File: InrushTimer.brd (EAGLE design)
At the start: 62.2 x 36 mm, 72 parts, among them IC1 TLC272D, IC2 555, IC3 4076N, Q2 TRANSISTOR-FET_2N7002, Q3 TRANSISTOR-FET_2N7002, Q4 TRANSISTOR-FET_2N7002, Q5 TRANSISTOR-FET_2N7002, Q6 DIODES_ZTX451DIODES_ZTX451_0_0, T1 MMBTA05, U1 ROHM_BY_ELEMENT14_BATCH_1_BU4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

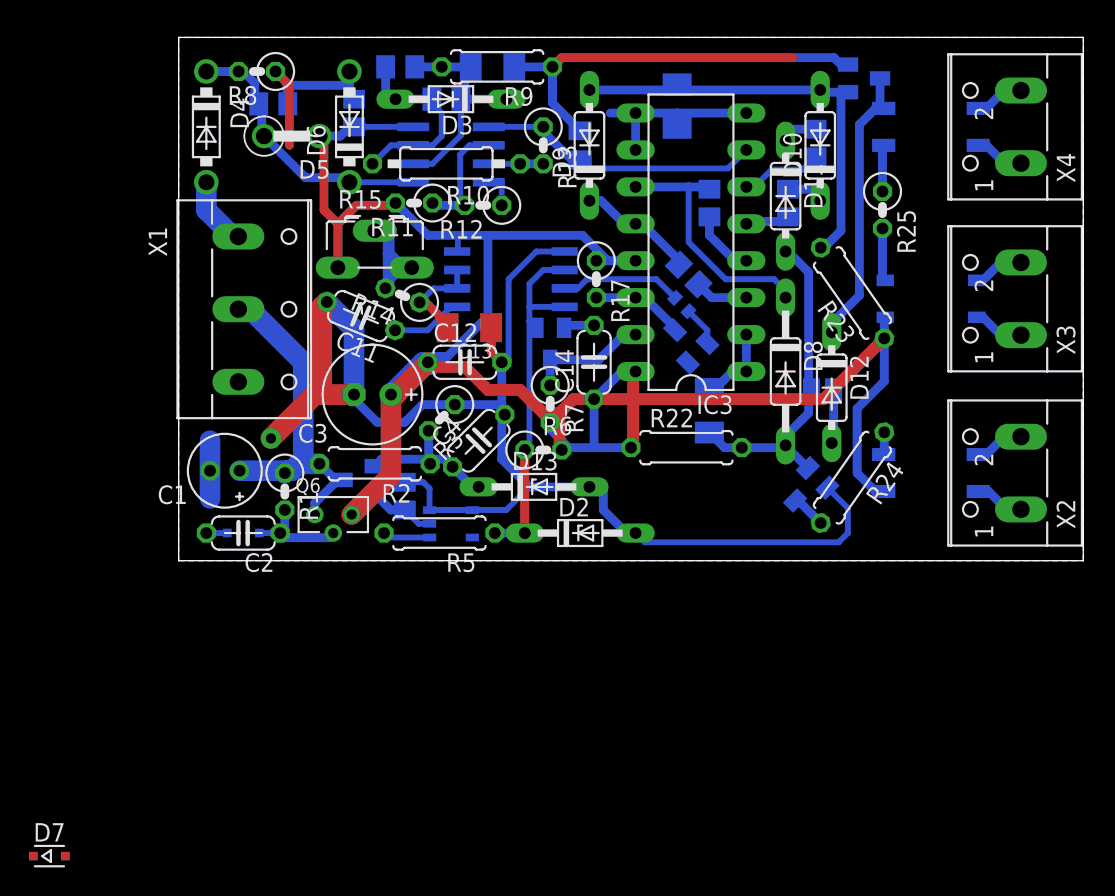
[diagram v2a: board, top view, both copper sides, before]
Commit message: Tidied up component and track placement.
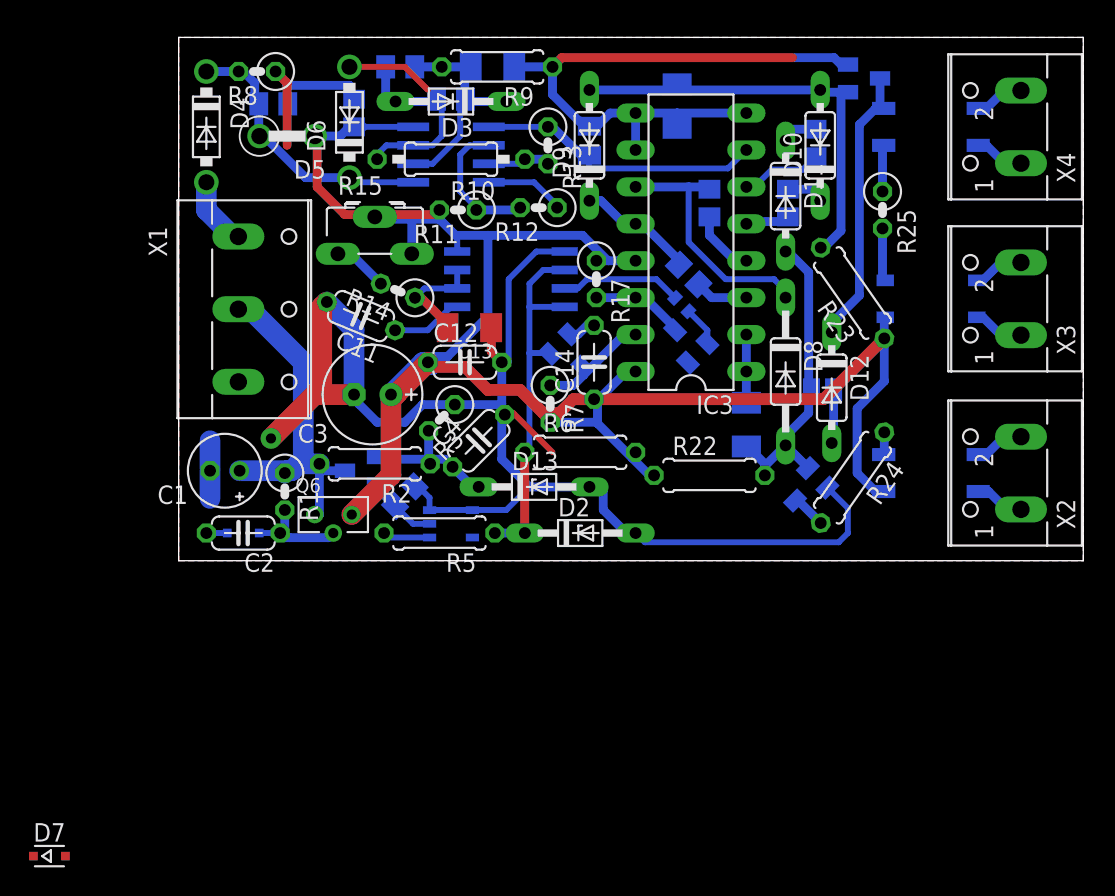
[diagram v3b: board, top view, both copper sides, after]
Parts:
- R6: device rcl:0207/2V -> rcl:0207/7
- moved R12 3.81 mm to (24.8, 24.3)
- moved R11 3.05 mm to (19.2, 24.1)
- moved C15 2.71 mm to (39.1, 9.37)
- moved R6 2.54 mm to (27.6, 7.46)
- moved R22 2.48 mm to (36.5, 5.87)
- moved Q2 1.63 mm to (27.0, 14.1), turned to 135 degrees
- moved R15 0.95 mm to (13.5, 21.1)
- moved C10 0.71 mm to (28.3, 28.9)
- moved T1 0.65 mm to (12.5, 6.19)
- moved R10 0.45 mm to (18.7, 27.6)
- moved R14 0.45 mm to (15.1, 18.6)
- moved C7 0.32 mm to (18.7, 31.8)
- moved D6 0.32 mm to (11.7, 30.2)
- moved D5 0.32 mm to (7.46, 29.2)
- moved R13 0.32 mm to (25.4, 28.6)
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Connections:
- removed net N$2: R14.2, R15.E, R15.S
- new net N$34: R14.2, R15.A
- net V12: now also R15.E, R15.S; no longer R15.A
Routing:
- net V12: track 153.5 -> 140.6 mm
- net ZERO: track 185.4 -> 195.3 mm
- net N$2: track 8.40 -> 0.00 mm
- net N$34: track 0.00 -> 3.80 mm
- net THRESH: track 8.14 -> 9.67 mm
- net ON_A_SYNC: track 22.9 -> 21.8 mm
- net RECT: track 24.0 -> 24.9 mm
- net RESET_N: track 25.3 -> 26.0 mm
- net N$28: track 7.04 -> 7.68 mm
- net N$26: track 3.75 -> 4.33 mm

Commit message: Rev two layout - minor change to track angle
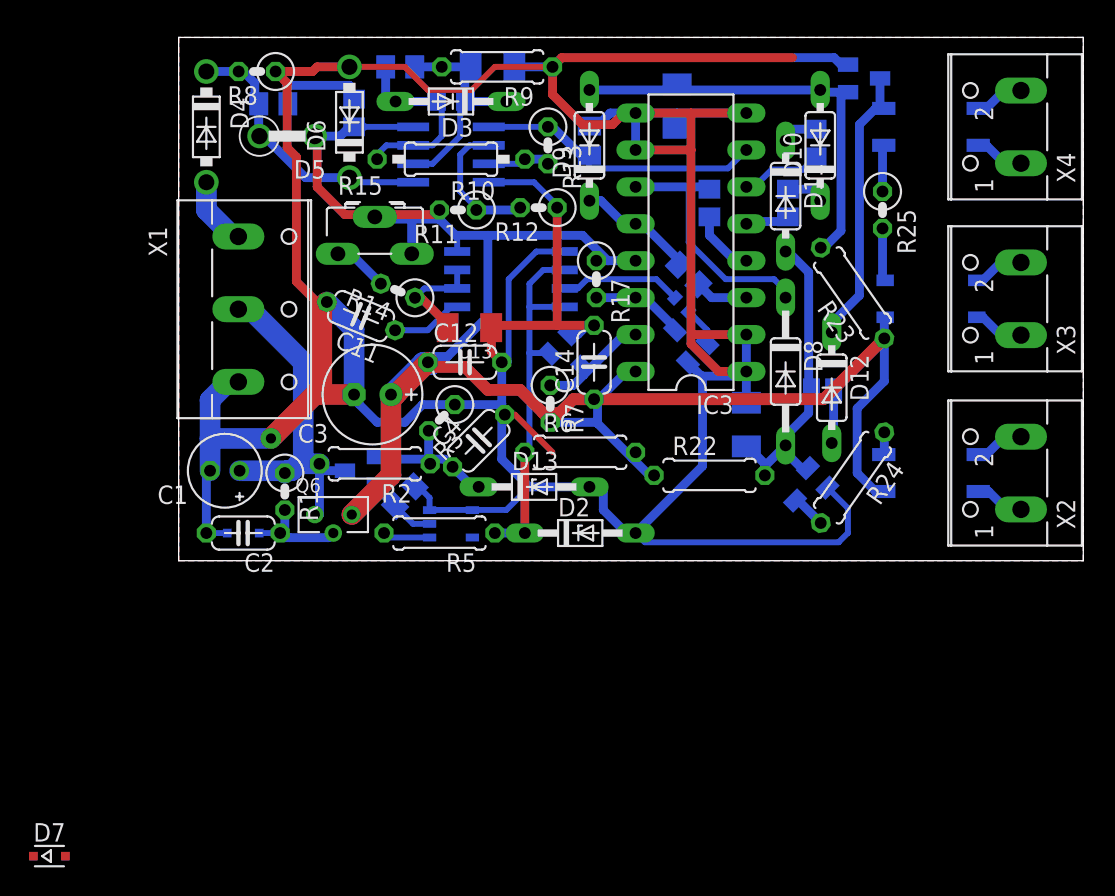
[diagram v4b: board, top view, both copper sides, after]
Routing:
- net ZERO: track 195.3 -> 312.0 mm
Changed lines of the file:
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@@
 <grid distance="0.05" unitdist="inch" unit="inch" style="lines" multiple="1" display="no" altdistance="0.00625" altunitdist="inch" altunit="inch"/>
 <layers>
-<layer number="1" name="Top" color="4" fill="1" visible="no" active="yes"/>
+<layer number="1" name="Top" color="4" fill="1" visible="yes" active="yes"/>
 <layer number="2" name="Route2" color="1" fill="3" visible="no" active="no"/>
 <layer number="3" name="Route3" color="4" fill="3" visible="no" active="no"/>
@@
 <layer number="20" name="Dimension" color="24" fill="1" visible="yes" active="yes"/>
 <layer number="21" name="tPlace" color="15" fill="1" visible="yes" active="yes"/>
-<layer number="22" name="bPlace" color="14" fill="1" visible="yes" active="yes"/>
-<layer number="23" name="tOrigins" color="15" fill="1" visible="yes" active="yes"/>
-<layer number="24" name="bOrigins" color="15" fill="1" visible="yes" active="yes"/>
+<layer number="22" name="bPlace" color="14" fill="1" visible="no" active="yes"/>
+<layer number="23" name="tOrigins" color="15" fill="1" visible="no" active="yes"/>
+<layer number="24" name="bOrigins" color="15" fill="1" visible="no" active="yes"/>
 <layer number="25" name="tNames" color="7" fill="1" visible="no" active="yes"/>
 <layer number="26" name="bNames" color="7" fill="1" visible="no" active="yes"/>
@@
 <layer number="46" name="Milling" color="3" fill="1" visible="no" active="yes"/>
 <layer number="47" name="Measures" color="7" fill="1" visible="no" active="yes"/>
-<layer number="48" name="Document" color="7" fill="1" visible="no" active="yes"/>
+<layer number="48" name="Document" color="7" fill="1" visible="yes" active="yes"/>
 <layer number="49" name="Reference" color="7" fill="1" visible="no" active="yes"/>
 <layer number="50" name="dxf" color="7" fill="1" visible="no" active="no"/>
-<layer number="51" name="tDocu" color="6" fill="1" visible="no" active="yes"/>
-<layer number="52" name="bDocu" color="7" fill="1" visible="no" active="yes"/>
+<layer number="51" name="tDocu" color="6" fill="1" visible="yes" active="yes"/>
+<layer number="52" name="bDocu" color="7" fill="1" visible="yes" active="yes"/>
 <layer number="53" name="tGND_GNDA" color="7" fill="9" visible="no" active="no"/>
 <layer number="54" name="bGND_GNDA" color="1" fill="9" visible="no" active="no"/>
@@
 <rectangle x1="49.53" y1="0" x2="62.23" y2="36" layer="42"/>
 <rectangle x1="49.53" y1="0" x2="62.23" y2="36" layer="41"/>
-<rectangle x1="0" y1="19.05" x2="6.35" y2="36" layer="41"/>
+<rectangle x1="0" y1="27.94" x2="5.3975" y2="36" layer="41"/>
 <rectangle x1="0" y1="19.05" x2="9.144" y2="30.48" layer="42"/>
+<rectangle x1="0" y1="19.05" x2="6.985" y2="27.94" layer="41"/>
 </plain>
 <attributes>
@@
 <wire x1="22.70125" y1="19.3675" x2="24.60625" y2="21.2725" width="0.4064" layer="16"/>
 <wire x1="24.60625" y1="21.2725" x2="26.56" y2="21.2725" width="0.4064" layer="16"/>
-<wire x1="7.46125" y1="32.86125" x2="7.46125" y2="28.575" width="0.6096" layer="1"/>
+<wire x1="7.46125" y1="32.86125" x2="7.46125" y2="28.41625" width="0.6096" layer="1"/>
 <wire x1="6.6675" y1="33.655" x2="7.46125" y2="32.86125" width="0.6096" layer="16"/>
 <wire x1="7.46125" y1="32.7025" x2="7.46125" y2="31.4325" width="0.6096" layer="16"/>
@@
 <wire x1="10.19459375" y1="17.799515625" x2="12.065" y2="15.929109375" width="1.4224" layer="16"/>
 <wire x1="12.065" y1="15.929109375" x2="12.065" y2="11.43" width="1.4224" layer="16"/>
-<wire x1="2.159" y1="6.35" x2="2.159" y2="8.255" width="1.4224" layer="16"/>
-<wire x1="2.159" y1="4.28625" x2="2.159" y2="6.19125" width="1.4224" layer="16"/>
-<wire x1="23.01875" y1="10.16" x2="25.7175" y2="7.46125" width="0.4064" layer="1"/>
-<wire x1="23.01875" y1="10.16" x2="22.86" y2="10.16" width="0.4064" layer="1"/>
+<wire x1="23.1277" y1="10.05105" x2="25.7175" y2="7.46125" width="0.4064" layer="1"/>
 <wire x1="29.68625" y1="30.7975" x2="28.78125" y2="29.8925" width="0.6096" layer="16"/>
 <wire x1="28.78125" y1="29.8925" x2="28.2575" y2="29.8925" width="0.6096" layer="16"/>
@@
 <wire x1="17.2593" y1="3.4798" x2="17.272" y2="3.4925" width="0.4064" layer="16"/>
 <wire x1="17.272" y1="3.4925" x2="22.5425" y2="3.4925" width="0.4064" layer="16"/>
+<wire x1="2.159" y1="8.41375" x2="2.159" y2="11.049" width="1.4224" layer="16"/>
+<wire x1="2.159" y1="11.049" x2="3.41375" y2="12.30375" width="1.4224" layer="16"/>
+<wire x1="3.41375" y1="12.30375" x2="4.1075" y2="12.30375" width="1.4224" layer="16"/>
+<wire x1="6.35" y1="8.41375" x2="2.159" y2="8.41375" width="1.4224" layer="16"/>
+<wire x1="39.0525" y1="13.0175" x2="39.0525" y2="12.7" width="0.6096" layer="16"/>
+<wire x1="39.0525" y1="12.7" x2="36.03625" y2="12.7" width="0.6096" layer="16"/>
+<wire x1="36.03625" y1="12.7" x2="35.962746875" y2="12.7" width="0.6096" layer="16"/>
+<wire x1="35.962746875" y1="12.7" x2="35.03106875" y2="13.631678125" width="0.6096" layer="16"/>
+<wire x1="31.4325" y1="1.905" x2="36.03625" y2="6.50875" width="0.6096" layer="16"/>
+<wire x1="36.03625" y1="6.50875" x2="36.03625" y2="12.7" width="0.6096" layer="16"/>
+<wire x1="25.7175" y1="33.9725" x2="25.7175" y2="32.0675" width="0.6096" layer="1"/>
+<wire x1="28.575" y1="16.1925" x2="26.035" y2="16.1925" width="0.6096" layer="1"/>
+<wire x1="26.035" y1="16.1925" x2="21.5025" y2="16.1925" width="0.6096" layer="1"/>
+<wire x1="21.5025" y1="16.1925" x2="21.5025" y2="16.03375" width="0.6096" layer="1"/>
+<wire x1="7.46125" y1="28.41625" x2="8.09625" y2="27.78125" width="0.6096" layer="1"/>
+<wire x1="8.09625" y1="27.78125" x2="8.09625" y2="19.20875" width="0.6096" layer="1"/>
+<wire x1="8.09625" y1="19.20875" x2="9.8425" y2="17.4625" width="0.6096" layer="1"/>
+<wire x1="11.7475" y1="33.9725" x2="9.525" y2="33.9725" width="0.6096" layer="1"/>
+<wire x1="9.525" y1="33.9725" x2="9.2075" y2="33.655" width="0.6096" layer="1"/>
+<wire x1="9.2075" y1="33.655" x2="6.6675" y2="33.655" width="0.6096" layer="1"/>
+<wire x1="35.2425" y1="28.2575" x2="35.2425" y2="14.9225" width="0.6096" layer="1"/>
+<wire x1="31.4325" y1="28.2575" x2="35.2425" y2="28.2575" width="0.6096" layer="1"/>
+<wire x1="31.4325" y1="30.7975" x2="35.2425" y2="30.7975" width="0.6096" layer="1"/>
+<wire x1="35.2425" y1="30.7975" x2="39.0525" y2="30.7975" width="0.6096" layer="1"/>
+<wire x1="39.0525" y1="30.7975" x2="39.37" y2="30.48" width="0.6096" layer="1"/>
+<wire x1="35.2425" y1="28.2575" x2="35.2425" y2="30.7975" width="0.6096" layer="1"/>
+<wire x1="39.0525" y1="13.0175" x2="37.1475" y2="13.0175" width="0.6096" layer="1"/>
+<wire x1="37.1475" y1="13.0175" x2="35.2425" y2="14.9225" width="0.6096" layer="1"/>
+<wire x1="39.0525" y1="15.5575" x2="35.40125" y2="15.5575" width="0.6096" layer="1"/>
+<wire x1="25.7175" y1="33.9725" x2="21.74875" y2="33.9725" width="0.4064" layer="1"/>
+<wire x1="21.74875" y1="33.9725" x2="20.16125" y2="32.385" width="0.4064" layer="1"/>
+<wire x1="20.16125" y1="32.385" x2="17.145" y2="32.385" width="0.4064" layer="1"/>
+<wire x1="25.7175" y1="32.0675" x2="27.78125" y2="30.00375" width="0.6096" layer="1"/>
+<wire x1="27.78125" y1="30.00375" x2="29.845" y2="30.00375" width="0.6096" layer="1"/>
+<wire x1="29.845" y1="30.00375" x2="30.63875" y2="30.7975" width="0.6096" layer="1"/>
+<wire x1="30.63875" y1="30.7975" x2="31.4325" y2="30.7975" width="0.6096" layer="1"/>
+<wire x1="26.035" y1="24.28875" x2="26.035" y2="16.1925" width="0.6096" layer="1"/>
+<wire x1="23.1277" y1="10.05105" x2="22.43355" y2="10.05105" width="0.4064" layer="1"/>
+<wire x1="2.159" y1="8.41375" x2="2.159" y2="6.19125" width="1.4224" layer="16"/>
+<wire x1="1.905" y1="1.905" x2="1.905" y2="6.19125" width="0.6096" layer="16"/>
+<wire x1="1.905" y1="6.19125" x2="2.159" y2="6.19125" width="0.6096" layer="16"/>
 </signal>
 <signal name="N$9">
@@
 <wire x1="41.91" y1="21.2725" x2="41.75125" y2="21.2725" width="0.6096" layer="16"/>
 <wire x1="43.28606875" y1="6.37081875" x2="43.28606875" y2="6.40268125" width="0.6096" layer="16"/>
-<wire x1="43.28606875" y1="6.40268125" x2="41.75125" y2="7.9375" width="0.6096" layer="16"/>
 <wire x1="40.3225" y1="6.6675" x2="39.12375" y2="7.86625" width="0.6096" layer="16"/>
 <wire x1="39.12375" y1="7.86625" x2="39.0525" y2="7.86625" width="0.6096" layer="16"/>
 <wire x1="40.3225" y1="6.6675" x2="40.3225" y2="6.50875" width="0.6096" layer="16"/>
-<wire x1="40.3225" y1="6.35" x2="40.3225" y2="5.87375" width="0.6096" layer="16"/>
+<wire x1="40.3225" y1="6.50875" x2="40.3225" y2="5.87375" width="0.6096" layer="16"/>
 <wire x1="41.75125" y1="7.9375" x2="40.3225" y2="6.50875" width="0.6096" layer="16"/>
-<wire x1="40.3225" y1="6.50875" x2="40.3225" y2="6.35" width="0.6096" layer="16"/>
+<wire x1="43.28606875" y1="6.40268125" x2="42.80981875" y2="6.40268125" width="0.6096" layer="16"/>
+<wire x1="42.80981875" y1="6.40268125" x2="41.75125" y2="7.46125" width="0.6096" layer="16"/>
+<wire x1="41.75125" y1="7.46125" x2="41.75125" y2="7.9375" width="0.6096" layer="16"/>
 </signal>
 <signal name="ON_B_SYNC">

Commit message: Changed pass element to TIP41C and moved some components around to make more space.
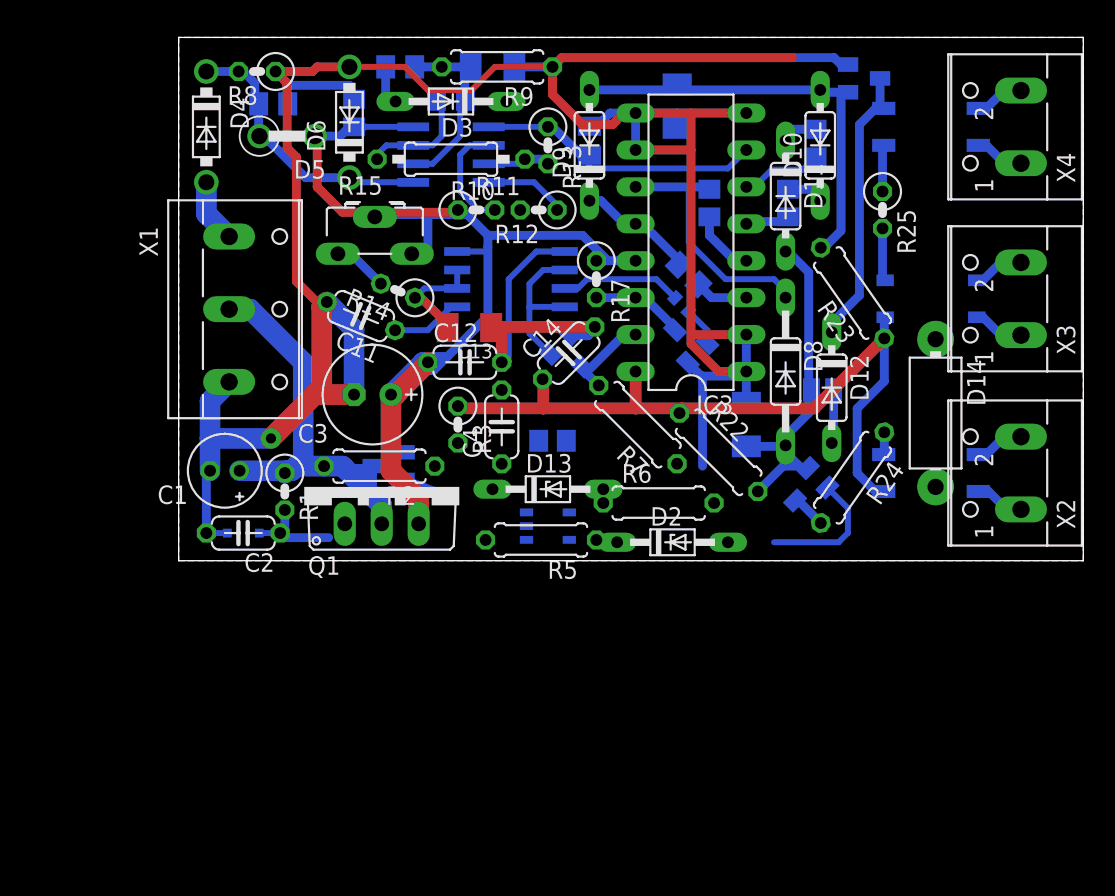
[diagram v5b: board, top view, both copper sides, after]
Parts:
- removed D7: (no value), diode:SOD323-R
- removed Q6: DIODES_ZTX451DIODES_ZTX451_0_0, Diodes - ZTX451:DIODES_ZTX451_0
- added D14: P6KEXXCTS-P6KE, diode:DO15-10
- added Q1: TIP41C, transistor-power:TO220AV
- R7: device rcl:0207/2V -> rcl:0207/7
- moved R4 10.9 mm to (25.7, 8.26), turned to 0 degrees
- moved R5 7.00 mm to (24.9, 1.43)
- moved U1 6.67 mm to (25.4, 2.38)
- moved R6 6.43 mm to (33.0, 3.97)
- moved D2 6.38 mm to (34.0, 1.27)
- moved R7 6.20 mm to (31.6, 9.37), turned to 135 degrees
- moved T1 1.93 mm to (14.4, 6.51)
- moved C14 1.86 mm to (26.8, 14.3), turned to 45 degrees
- moved C4 1.85 mm to (22.2, 9.21), turned to 90 degrees
- moved R22 1.71 mm to (37.1, 7.46), turned to 315 degrees
- moved R11 1.27 mm to (20.5, 24.1), turned to 0 degrees
- moved R3 1.21 mm to (19.2, 9.37), turned to 270 degrees
- moved D13 0.97 mm to (25.4, 4.92)
- moved X1 0.63 mm to (4.76, 17.3)
- moved R2 0.35 mm to (13.8, 6.51)
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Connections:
- net N$8: now also Q1.B; no longer Q6.2
- net RECT: now also Q1.C; no longer Q6.3
- net RESET: now also R7.2; no longer R7.1
- net THRESH: now also R11.2; no longer R11.1
- net V12: now also D14.C, Q1.E, R11.1, R7.1; no longer Q6.1, R11.2, R7.2
- net ZERO: now also D14.A
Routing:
- net ZERO: track 312.0 -> 241.5 mm
- net RESET_N: track 26.0 -> 10.7 mm
- net N$14: track 10.6 -> 0.00 mm
- net V12: track 140.6 -> 130.8 mm
- net RECT: track 24.9 -> 31.8 mm
- net N$23: track 3.26 -> 0.00 mm
- net THRESH: track 9.67 -> 7.68 mm
- net N$13: track 4.87 -> 3.08 mm
- net ON_A_SYNC: track 22.0 -> 23.8 mm
- net RESET: track 7.93 -> 6.30 mm
